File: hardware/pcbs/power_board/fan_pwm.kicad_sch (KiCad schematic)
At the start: 5 parts, among them Q8 IRML6401, U11 4069

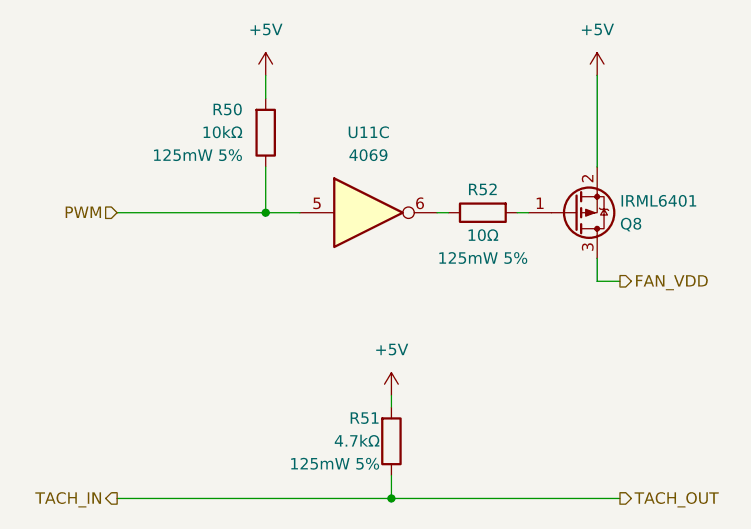
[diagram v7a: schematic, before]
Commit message: power_board: add capacitors for filtering fan power supply
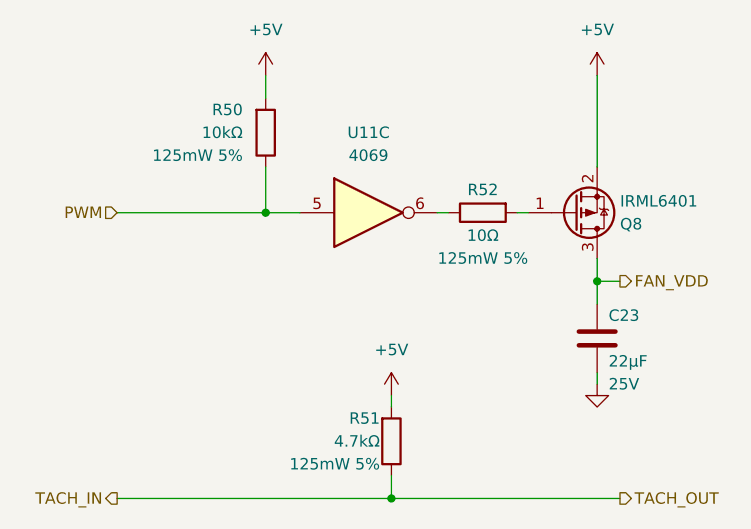
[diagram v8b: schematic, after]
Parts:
- added C23: 22μF, Capacitor_SMD:C_0805_2012Metric, symbol Device:C
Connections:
- net FAN_VDD: now also C23.1
- new net GND: C23.2
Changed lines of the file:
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@@
 	(paper "A4")
+	(junction
+		(at 168.91 99.06)
+		(diameter 0)
+		(color 0 0 0 0)
+	)
 	(junction
 		(at 146.05 123.19)
@@
 	(wire
 		(pts
+			(xy 168.91 109.22) (xy 168.91 110.49)
+		)
+		(stroke
+			(width 0)
+			(type default)
+		)
+	)
+	(wire
+		(pts
 			(xy 132.08 91.44) (xy 135.89 91.44)
 		)
@@
 		(pts
 			(xy 132.08 76.2) (xy 132.08 78.74)
+		)
+		(stroke
+			(width 0)
+			(type default)
+		)
+	)
+	(wire
+		(pts
+			(xy 168.91 99.06) (xy 168.91 101.6)
 		)
 		(stroke
@@
 	)
 	(symbol
+		(lib_id "power:GND")
+		(at 168.91 110.49 0)
+		(unit 1)
+		(exclude_from_sim no)
+		(in_bom yes)
+		(on_board yes)
+		(dnp no)
+		(fields_autoplaced yes)
+		(property "Reference" "#PWR055"
+			(at 168.91 116.84 0)
+			(effects
+				(font
+					(size 1.27 1.27)
+				)
+				(hide yes)
+			)
+		)
+		(property "Value" "GND"
+			(at 168.91 115.57 0)
+			(effects
+				(font
+					(size 1.27 1.27)
+				)
+				(hide yes)
+			)
+		)
+		(property "Footprint" ""
+			(at 168.91 110.49 0)
+			(effects
+				(font
+					(size 1.27 1.27)
+				)
+				(hide yes)
+			)
+		)
+		(property "Datasheet" ""
+			(at 168.91 110.49 0)
+			(effects
+				(font
+					(size 1.27 1.27)
+				)
+				(hide yes)
+			)
+		)
+		(property "Description" ""
+			(at 168.91 110.49 0)
+			(effects
+				(font
+					(size 1.27 1.27)
+				)
+				(hide yes)
+			)
+		)
+		(pin "1"
+		)
+		(instances
+			(project "power_board"
+				(path "/4b166175-80a4-48c6-994d-6e62a6160b87/f4395b92-97ec-456a-b4c2-238b75f494a2/06607c2e-df57-4ef0-bf70-954d4a07371a"
+					(reference "#PWR0100")
+					(unit 1)
+				)
+				(path "/4b166175-80a4-48c6-994d-6e62a6160b87/f4395b92-97ec-456a-b4c2-238b75f494a2/1f2356c2-5114-44bd-9e00-8022e0f5b6a5"
+					(reference "#PWR055")
+					(unit 1)
+				)
+				(path "/4b166175-80a4-48c6-994d-6e62a6160b87/f4395b92-97ec-456a-b4c2-238b75f494a2/67d89172-f710-42f2-b66a-20a713f3ef78"
+					(reference "#PWR096")
+					(unit 1)
+				)
+				(path "/4b166175-80a4-48c6-994d-6e62a6160b87/f4395b92-97ec-456a-b4c2-238b75f494a2/ba1e0391-72e2-478c-ae36-437899b49871"
+					(reference "#PWR059")
+					(unit 1)
+				)
+			)
+		)
+	)
+	(symbol
 		(lib_id "Device:R")
 		(at 156.21 91.44 90)
@@
 				)
 				(path "/4b166175-80a4-48c6-994d-6e62a6160b87/f4395b92-97ec-456a-b4c2-238b75f494a2/1f2356c2-5114-44bd-9e00-8022e0f5b6a5"
-					(reference "#PWR054")
+					(reference "#PWR053")
 					(unit 1)
 				)
 				(path "/4b166175-80a4-48c6-994d-6e62a6160b87/f4395b92-97ec-456a-b4c2-238b75f494a2/67d89172-f710-42f2-b66a-20a713f3ef78"
-					(reference "#PWR095")
+					(reference "#PWR094")
 					(unit 1)
 				)
@@
 	)
 	(symbol
+		(lib_id "Device:C")
+		(at 168.91 105.41 0)
+		(unit 1)
+		(exclude_from_sim no)
+		(in_bom yes)
+		(on_board yes)
+		(dnp no)
+		(property "Reference" "C23"
+			(at 170.18 102.87 0)
+			(effects
+				(font
+					(size 1.27 1.27)
+				)
+				(justify left)
+			)
+		)
+		(property "Value" "22μF"
+			(at 170.18 107.95 0)
+			(effects
+				(font
+					(size 1.27 1.27)
+				)
+				(justify left)
+			)
+		)
+		(property "Footprint" "Capacitor_SMD:C_0805_2012Metric"
+			(at 169.8752 109.22 0)
+			(effects
+				(font
+					(size 1.27 1.27)
+				)
+				(hide yes)
+			)
+		)
+		(property "Datasheet" "~"
+			(at 168.91 105.41 0)
+			(effects
+				(font
+					(size 1.27 1.27)
+				)
+				(hide yes)
+			)
+		)
+		(property "Description" ""
+			(at 168.91 105.41 0)
+			(effects
+				(font
+					(size 1.27 1.27)
+				)
+				(hide yes)
+			)
+		)
+		(property "Info" "25V"
+			(at 170.18 110.49 0)
+			(effects
+				(font
+					(size 1.27 1.27)
+				)
+				(justify left)
+			)
+		)
+		(property "Shop" "https://store.comet.bg/Catalogue/Product/37065/"
+			(at 168.91 105.41 0)
+			(effects
+				(font
+					(size 1.27 1.27)
+				)
+				(hide yes)
+			)
+		)
+		(property "LCSC" ""
+			(at 168.91 105.41 0)
+			(effects
+				(font
+					(size 1.27 1.27)
+				)
+				(hide yes)
+			)
+		)
+		(property "Part" "C 22μF 25V 0805"
+			(at 168.91 105.41 0)
+			(effects
+				(font
+					(size 1.27 1.27)
+				)
+				(hide yes)
+			)
+		)
+		(pin "1"
+		)
+		(pin "2"
+		)
+		(instances
+			(project "power_board"
+				(path "/4b166175-80a4-48c6-994d-6e62a6160b87/f4395b92-97ec-456a-b4c2-238b75f494a2/06607c2e-df57-4ef0-bf70-954d4a07371a"
+					(reference "C37")
+					(unit 1)
+				)
+				(path "/4b166175-80a4-48c6-994d-6e62a6160b87/f4395b92-97ec-456a-b4c2-238b75f494a2/1f2356c2-5114-44bd-9e00-8022e0f5b6a5"
+					(reference "C23")
+					(unit 1)
+				)
+				(path "/4b166175-80a4-48c6-994d-6e62a6160b87/f4395b92-97ec-456a-b4c2-238b75f494a2/67d89172-f710-42f2-b66a-20a713f3ef78"
+					(reference "C36")
+					(unit 1)
+				)
+				(path "/4b166175-80a4-48c6-994d-6e62a6160b87/f4395b92-97ec-456a-b4c2-238b75f494a2/ba1e0391-72e2-478c-ae36-437899b49871"
+					(reference "C24")
+					(unit 1)
+				)
+			)
+		)
+	)
+	(symbol
 		(lib_id "power:+5V")
 		(at 168.91 76.2 0)
@@
 				)
 				(path "/4b166175-80a4-48c6-994d-6e62a6160b87/f4395b92-97ec-456a-b4c2-238b75f494a2/1f2356c2-5114-44bd-9e00-8022e0f5b6a5"
-					(reference "#PWR055")
+					(reference "#PWR054")
 					(unit 1)
 				)
 				(path "/4b166175-80a4-48c6-994d-6e62a6160b87/f4395b92-97ec-456a-b4c2-238b75f494a2/67d89172-f710-42f2-b66a-20a713f3ef78"
-					(reference "#PWR096")
+					(reference "#PWR095")
 					(unit 1)
 				)
@@
 				)
 				(path "/4b166175-80a4-48c6-994d-6e62a6160b87/f4395b92-97ec-456a-b4c2-238b75f494a2/1f2356c2-5114-44bd-9e00-8022e0f5b6a5"
-					(reference "#PWR053")
+					(reference "#PWR052")
 					(unit 1)
 				)
 				(path "/4b166175-80a4-48c6-994d-6e62a6160b87/f4395b92-97ec-456a-b4c2-238b75f494a2/67d89172-f710-42f2-b66a-20a713f3ef78"
-					(reference "#PWR094")
-					(unit 1)
-				)
+					(reference "#PWR093")
+					(unit 1)
+				)
